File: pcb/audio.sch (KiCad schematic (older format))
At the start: 32 parts, among them J1 AudioJack3_SwitchTR, U400 CS43130, U401 ADP150-3.0, U402 ADP150-1.8, U403 ADP150-1.8, X400 DSC1001CE2-022.5792

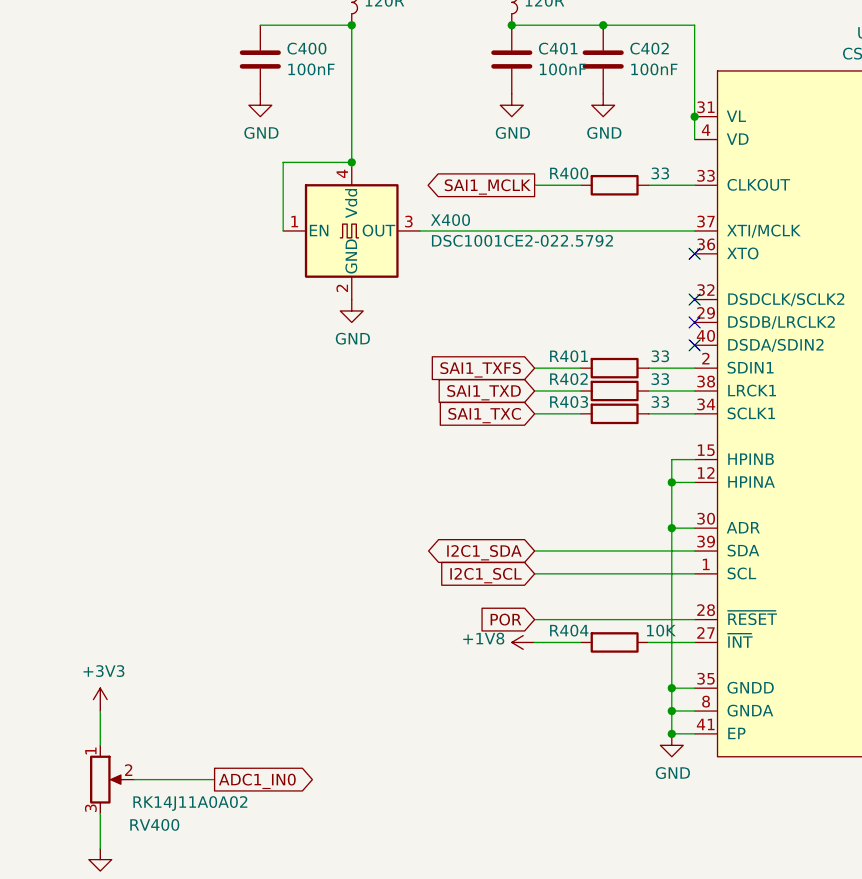
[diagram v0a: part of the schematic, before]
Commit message: pcb: adding lpc5500
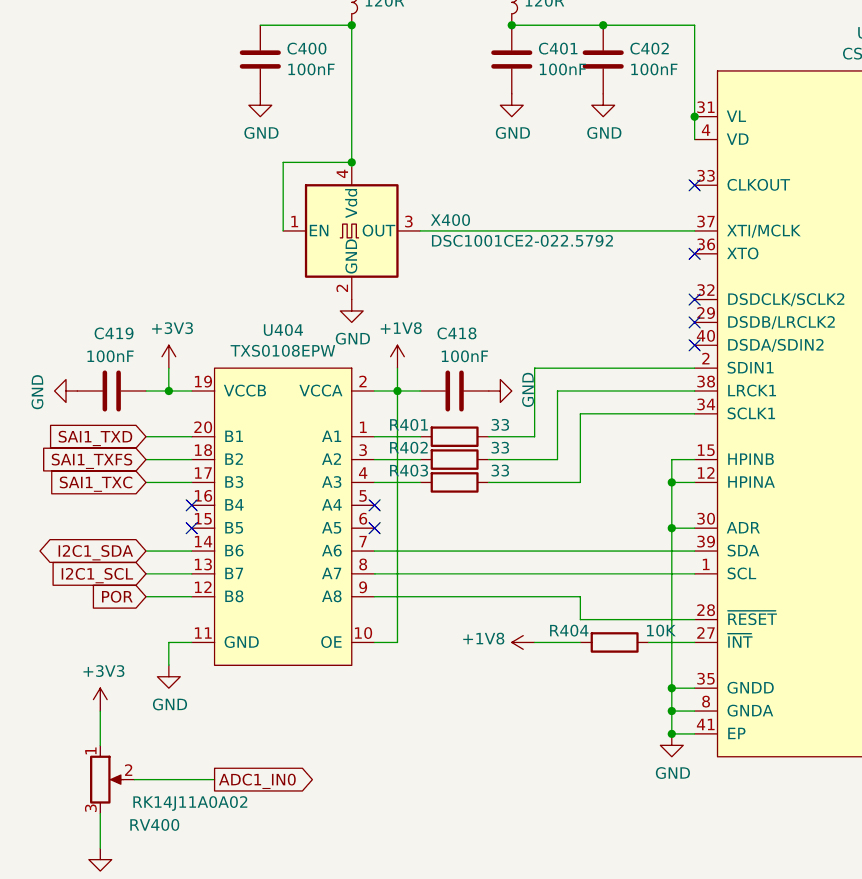
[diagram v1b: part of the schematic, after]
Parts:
- removed R400: 33, Resistor_SMD:R_0603_1608Metric, symbol Device:R
- added C418, C419: 100nF, Capacitor_SMD:C_0402_1005Metric, symbol Device:C
- added U404: TXS0108EPW, Package_SO:TSSOP-20_4.4x6.5mm_P0.65mm, symbol symbols:TXS0108EPW
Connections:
- net +1V8: now also C418.1, U404.10 (OE), U404.2 (VCCA)
- net +3V3: now also C419.2, U404.19 (VCCB)
- net GND: now also C418.2, C419.1, U404.11 (GND)
- net I2C1_SCL: now also U404.13 (B7); no longer U400.1 (SCL)
- net I2C1_SDA: now also U404.14 (B6); no longer U400.39 (SDA)
- net POR: now also U404.12 (B8); no longer U400.28 (~RESET)
- net SAI1_TXC: now also U404.17 (B3); no longer R403.2
- net SAI1_TXD: now also U404.20 (B1); no longer R402.2
- net SAI1_TXFS: now also U404.18 (B2); no longer R401.2
- new net: U400.1 (SCL), U404.8 (A7)
- new net: U400.28 (~RESET), U404.9 (A8)
- new net: U400.39 (SDA), U404.7 (A6)
- new net: R401.2, U404.1 (A1)
- new net: R402.2, U404.3 (A2)
- new net: R403.2, U404.4 (A3)
- no-connect marks 4 -> 9
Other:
- moved on the sheet: R401, R402, R403
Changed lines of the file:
@@
 $Descr A4 11693 8268
 encoding utf-8
-Sheet 7 11
-Title "RhythmPocket"
-Date "2019-08-12"
-Rev "R0.2"
+Sheet 6 8
+Title "RhythmPocketLite"
+Date "2019-09-06"
+Rev "R0.1"
 Comp "ZephRay"
 Comment1 "zephray@outlook.com"
@@
 Comment4 ""
 $EndDescr
-Text GLabel 4300 4300 0    50   Input ~ 0
+Text GLabel 2600 4600 0    50   Input ~ 0
 SAI1_TXC
-Text GLabel 4300 4100 0    50   Input ~ 0
+Text GLabel 2600 4500 0    50   Input ~ 0
 SAI1_TXFS
-Text GLabel 4300 4200 0    50   Input ~ 0
+Text GLabel 2600 4400 0    50   Input ~ 0
 SAI1_TXD
 $Comp
@@
 	4200 2600 4600 2600
 Connection ~ 4200 2600
-Text GLabel 4300 3300 0    50   Output ~ 0
-SAI1_MCLK
-$Comp
-L Device:R R400
-U 1 1 5D42CABC
-P 4650 3300
-F 0 "R400" V 4600 3100 50  0000 C CNN
-F 1 "33" V 4600 3500 50  0000 C CNN
-F 2 "Resistor_SMD:R_0603_1608Metric" V 4580 3300 50  0001 C CNN
-F 3 "~" H 4650 3300 50  0001 C CNN
-	1    4650 3300
-	0    1    1    0
-$EndComp
 $Comp
 L Device:R R401
 U 1 1 5D437A63
-P 4650 4100
-F 0 "R401" V 4600 3900 50  0000 C CNN
-F 1 "33" V 4600 4300 50  0000 C CNN
-F 2 "Resistor_SMD:R_0603_1608Metric" V 4580 4100 50  0001 C CNN
-F 3 "~" H 4650 4100 50  0001 C CNN
-	1    4650 4100
+P 3950 4400
+F 0 "R401" V 3900 4200 50  0000 C CNN
+F 1 "33" V 3900 4600 50  0000 C CNN
+F 2 "Resistor_SMD:R_0603_1608Metric" V 3880 4400 50  0001 C CNN
+F 3 "~" H 3950 4400 50  0001 C CNN
+	1    3950 4400
 	0    1    1    0
 $EndComp
@@
 L Device:R R402
 U 1 1 5D438FF1
-P 4650 4200
-F 0 "R402" V 4600 4000 50  0000 C CNN
-F 1 "33" V 4600 4400 50  0000 C CNN
-F 2 "Resistor_SMD:R_0603_1608Metric" V 4580 4200 50  0001 C CNN
-F 3 "~" H 4650 4200 50  0001 C CNN
-	1    4650 4200
+P 3950 4500
+F 0 "R402" V 3900 4300 50  0000 C CNN
+F 1 "33" V 3900 4700 50  0000 C CNN
+F 2 "Resistor_SMD:R_0603_1608Metric" V 3880 4500 50  0001 C CNN
+F 3 "~" H 3950 4500 50  0001 C CNN
+	1    3950 4500
 	0    1    1    0
 $EndComp
@@
 L Device:R R403
 U 1 1 5D4391CB
-P 4650 4300
-F 0 "R403" V 4600 4100 50  0000 C CNN
-F 1 "33" V 4600 4500 50  0000 C CNN
-F 2 "Resistor_SMD:R_0603_1608Metric" V 4580 4300 50  0001 C CNN
-F 3 "~" H 4650 4300 50  0001 C CNN
-	1    4650 4300
+P 3950 4600
+F 0 "R403" V 3900 4400 50  0000 C CNN
+F 1 "33" V 3900 4800 50  0000 C CNN
+F 2 "Resistor_SMD:R_0603_1608Metric" V 3880 4600 50  0001 C CNN
+F 3 "~" H 3950 4600 50  0001 C CNN
+	1    3950 4600
 	0    1    1    0
 $EndComp
@@
 	5000 3000 5000 3100
 Wire Wire Line
-	4300 4100 4500 4100
-Wire Wire Line
-	4300 4200 4500 4200
-Wire Wire Line
-	4300 4300 4500 4300
-Wire Wire Line
-	4300 3300 4500 3300
-Wire Wire Line
-	4800 3300 5000 3300
-Wire Wire Line
-	4800 4100 5000 4100
-Wire Wire Line
-	4800 4200 5000 4200
-Wire Wire Line
-	4800 4300 5000 4300
-$Comp
-L power:GND #PWR0270
-U 1 1 5D44FB8A
-P 4900 5700
-F 0 "#PWR0270" H 4900 5450 50  0001 C CNN
-F 1 "GND" H 4905 5527 50  0000 C CNN
-F 2 "" H 4900 5700 50  0001 C CNN
-F 3 "" H 4900 5700 50  0001 C CNN
-	1    4900 5700
-	1    0    0    -1
-$EndComp
+	3600 4400 3800 4400
+Wire Wire Line
+	3600 4500 3800 4500
+Wire Wire Line
+	3600 4600 3800 4600
+Wire Wire Line
+	4100 4400 4300 4400
 Wire Wire Line
 	5000 4800 4900 4800
@@
 Wire Wire Line
 	4900 5600 4900 5700
-Wire Wire Line
-	5000 4500 4900 4500
-Wire Wire Line
-	4900 4500 4900 4600
 Connection ~ 4900 4800
 Wire Wire Line
 	5000 4600 4900 4600
-Connection ~ 4900 4600
 Wire Wire Line
 	4900 4600 4900 4800
-Text GLabel 4300 5000 0    50   Input ~ 0
+Text GLabel 2600 5000 0    50   Input ~ 0
 I2C1_SCL
-Text GLabel 4300 4900 0    50   BiDi ~ 0
+Text GLabel 2600 4900 0    50   BiDi ~ 0
 I2C1_SDA
-Wire Wire Line
-	4300 4900 5000 4900
-Wire Wire Line
-	4300 5000 5000 5000
-Text GLabel 4300 5200 0    50   Input ~ 0
+Text GLabel 2600 5100 0    50   Input ~ 0
 POR
-Wire Wire Line
-	4300 5200 5000 5200
 $Comp
 L Device:R R404
@@
 Wire Wire Line
 	6600 5400 7650 5400
+NoConn ~ 5000 3300
+$Comp
+L symbols:TXS0108EPW U404
+U 1 1 5D795725
+P 3200 4400
+F 0 "U404" H 3200 4865 50  0000 C CNN
+F 1 "TXS0108EPW" H 3200 4774 50  0000 C CNN
+F 2 "Package_SO:TSSOP-20_4.4x6.5mm_P0.65mm" H 3200 4400 50  0001 C CNN
+F 3 "" H 3200 4400 50  0001 C CNN
+	1    3200 4400
+	-1   0    0    -1
+$EndComp
+Wire Wire Line
+	2600 4400 2800 4400
+Wire Wire Line
+	2600 4500 2800 4500
+Wire Wire Line
+	2600 4600 2800 4600
+Wire Wire Line
+	4300 4400 4300 4100
+Wire Wire Line
+	4300 4100 5000 4100
+Wire Wire Line
+	5000 4200 4400 4200
+Wire Wire Line
+	4400 4200 4400 4500
+Wire Wire Line
+	4100 4500 4400 4500
+Wire Wire Line
+	4500 4600 4500 4300
+Wire Wire Line
+	4500 4300 5000 4300
+Wire Wire Line
+	4100 4600 4500 4600
+Wire Wire Line
+	5000 4500 4900 4500
+Wire Wire Line
+	4900 4500 4900 4600
+Connection ~ 4900 4600
+Wire Wire Line
+	2600 4900 2800 4900
+Wire Wire Line
+	2600 5000 2800 5000
+Wire Wire Line
+	2600 5100 2800 5100
+Wire Wire Line
+	3600 4900 5000 4900
+Wire Wire Line
+	3600 5000 5000 5000
+Wire Wire Line
+	5000 5200 4500 5200
+Wire Wire Line
+	4500 5200 4500 5100
+Wire Wire Line
+	4500 5100 3600 5100
+NoConn ~ 3600 4700
+NoConn ~ 3600 4800
+NoConn ~ 2800 4700
+NoConn ~ 2800 4800
+$Comp
+L power:+1V8 #PWR?
+U 1 1 5D818AFA
+P 3700 4100
+F 0 "#PWR?" H 3700 3950 50  0001 C CNN
+F 1 "+1V8" H 3715 4273 50  0000 C CNN
+F 2 "" H 3700 4100 50  0001 C CNN
+F 3 "" H 3700 4100 50  0001 C CNN
+	1    3700 4100
+	1    0    0    -1
+$EndComp
+Wire Wire Line
+	3600 4200 3700 4200
+Wire Wire Line
+	3700 4200 3700 4100
+Wire Wire Line
+	3600 5300 3700 5300
+Wire Wire Line
+	3700 5300 3700 4200
+Connection ~ 3700 4200
+$Comp
+L power:+3V3 #PWR?
+U 1 1 5D825A06
+P 2700 4100
+F 0 "#PWR?" H 2700 3950 50  0001 C CNN
+F 1 "+3V3" H 2715 4273 50  0000 C CNN
+F 2 "" H 2700 4100 50  0001 C CNN
+F 3 "" H 2700 4100 50  0001 C CNN
+	1    2700 4100
+	1    0    0    -1
+$EndComp
+Wire Wire Line
+	2700 4100 2700 4200
+Wire Wire Line
+	2700 4200 2800 4200
+$Comp
+L power:GND #PWR0270
+U 1 1 5D44FB8A
+P 4900 5700
+F 0 "#PWR0270" H 4900 5450 50  0001 C CNN
+F 1 "GND" H 4905 5527 50  0000 C CNN
+F 2 "" H 4900 5700 50  0001 C CNN
+F 3 "" H 4900 5700 50  0001 C CNN
+	1    4900 5700
+	1    0    0    -1
+$EndComp
+$Comp
+L power:GND #PWR?
+U 1 1 5D830E8D
+P 2700 5400
+F 0 "#PWR?" H 2700 5150 50  0001 C CNN
+F 1 "GND" H 2705 5227 50  0000 C CNN
+F 2 "" H 2700 5400 50  0001 C CNN
+F 3 "" H 2700 5400 50  0001 C CNN
+	1    2700 5400
+	1    0    0    -1
+$EndComp
+Wire Wire Line
+	2800 5300 2700 5300
+Wire Wire Line
+	2700 5300 2700 5400
+$Comp
+L Device:C C418
+U 1 1 5D83653A
+P 3950 4200
+F 0 "C418" V 4200 4100 50  0000 L CNN
+F 1 "100nF" V 4100 4050 50  0000 L CNN
+F 2 "Capacitor_SMD:C_0402_1005Metric" H 3988 4050 50  0001 C CNN
+F 3 "~" H 3950 4200 50  0001 C CNN
+	1    3950 4200
+	0    -1   -1   0
+$EndComp
+$Comp
+L Device:C C419
+U 1 1 5D83DFEF
+P 2450 4200
+F 0 "C419" V 2700 4100 50  0000 L CNN
+F 1 "100nF" V 2600 4100 50  0000 L CNN
+F 2 "Capacitor_SMD:C_0402_1005Metric" H 2488 4050 50  0001 C CNN
+F 3 "~" H 2450 4200 50  0001 C CNN
+	1    2450 4200
+	0    -1   -1   0
+$EndComp
+Wire Wire Line
+	2600 4200 2700 4200
+Connection ~ 2700 4200
+Wire Wire Line
+	3800 4200 3700 4200
+$Comp
+L power:GND #PWR?
+U 1 1 5D84AB6D
+P 4100 4200
+F 0 "#PWR?" H 4100 3950 50  0001 C CNN
+F 1 "GND" H 4105 4027 50  0000 C CNN
+F 2 "" H 4100 4200 50  0001 C CNN
+F 3 "" H 4100 4200 50  0001 C CNN
+	1    4100 4200
+	0    -1   -1   0
+$EndComp
+$Comp
+L power:GND #PWR?
+U 1 1 5D84B27D
+P 2300 4200
+F 0 "#PWR?" H 2300 3950 50  0001 C CNN
+F 1 "GND" H 2305 4027 50  0000 C CNN
+F 2 "" H 2300 4200 50  0001 C CNN
+F 3 "" H 2300 4200 50  0001 C CNN
+	1    2300 4200
+	0    1    1    0
+$EndComp
 $EndSCHEMATC

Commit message: pcb: rev 0.1
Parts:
- removed C418, C419: 100nF, Capacitor_SMD:C_0402_1005Metric, symbol Device:C
- removed U404: TXS0108EPW, Package_SO:TSSOP-20_4.4x6.5mm_P0.65mm, symbol symbols:TXS0108EPW
- removed X400: DSC1001CE2-022.5792, Oscillator:Oscillator_SMD_Abracon_ASE-4Pin_3.2x2.5mm, symbol Oscillator:ASE-xxxMHz
- added R400: 33, Resistor_SMD:R_0603_1608Metric, symbol Device:R
- added X1: DSC1001CE2-022.5792, Oscillator:Oscillator_SMD_Abracon_ASE-4Pin_3.2x2.5mm, symbol Oscillator:ASE-xxxMHz
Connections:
- net +1V8: now also RV400.1
- net +3V3: no longer RV400.1
- net GND: now also X1.2 (GND)
- net I2C1_SCL: now also U400.1 (SCL)
- net I2C1_SDA: now also U400.39 (SDA)
- net POR: now also U400.28 (~RESET)
- net SAI1_TXC: now also R403.2
- net SAI1_TXD: now also R401.2
- net SAI1_TXFS: now also R402.2
- net at U400.33 (CLKOUT): now also R400.1
- net at U400.37 (XTI/MCLK): now also X1.3 (OUT)
- net at C400.1, L400.2: now also X1.1 (EN), X1.4 (Vdd)
- new net SAI1_MCLK: R400.2
- no-connect marks 9 -> 4
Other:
- moved on the sheet: R401, R402, R403
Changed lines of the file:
@@
 Comment4 ""
 $EndDescr
-Text GLabel 2600 4600 0    50   Input ~ 0
-SAI1_TXC
-Text GLabel 2600 4500 0    50   Input ~ 0
-SAI1_TXFS
-Text GLabel 2600 4400 0    50   Input ~ 0
-SAI1_TXD
 $Comp
 L symbols:CS43130 U400
@@
 L Device:R R401
 U 1 1 5D437A63
-P 3950 4400
-F 0 "R401" V 3900 4200 50  0000 C CNN
-F 1 "33" V 3900 4600 50  0000 C CNN
-F 2 "Resistor_SMD:R_0603_1608Metric" V 3880 4400 50  0001 C CNN
-F 3 "~" H 3950 4400 50  0001 C CNN
-	1    3950 4400
+P 3950 4100
+F 0 "R401" V 3900 3900 50  0000 C CNN
+F 1 "33" V 3900 4300 50  0000 C CNN
+F 2 "Resistor_SMD:R_0603_1608Metric" V 3880 4100 50  0001 C CNN
+F 3 "~" H 3950 4100 50  0001 C CNN
+	1    3950 4100
 	0    1    1    0
 $EndComp
@@
 L Device:R R402
 U 1 1 5D438FF1
-P 3950 4500
-F 0 "R402" V 3900 4300 50  0000 C CNN
-F 1 "33" V 3900 4700 50  0000 C CNN
-F 2 "Resistor_SMD:R_0603_1608Metric" V 3880 4500 50  0001 C CNN
-F 3 "~" H 3950 4500 50  0001 C CNN
-	1    3950 4500
+P 3950 4200
+F 0 "R402" V 3900 4000 50  0000 C CNN
+F 1 "33" V 3900 4400 50  0000 C CNN
+F 2 "Resistor_SMD:R_0603_1608Metric" V 3880 4200 50  0001 C CNN
+F 3 "~" H 3950 4200 50  0001 C CNN
+	1    3950 4200
 	0    1    1    0
 $EndComp
@@
 L Device:R R403
 U 1 1 5D4391CB
-P 3950 4600
-F 0 "R403" V 3900 4400 50  0000 C CNN
-F 1 "33" V 3900 4800 50  0000 C CNN
-F 2 "Resistor_SMD:R_0603_1608Metric" V 3880 4600 50  0001 C CNN
-F 3 "~" H 3950 4600 50  0001 C CNN
-	1    3950 4600
+P 3950 4300
+F 0 "R403" V 3900 4100 50  0000 C CNN
+F 1 "33" V 3900 4500 50  0000 C CNN
+F 2 "Resistor_SMD:R_0603_1608Metric" V 3880 4300 50  0001 C CNN
+F 3 "~" H 3950 4300 50  0001 C CNN
+	1    3950 4300
 	0    1    1    0
 $EndComp
@@
 	5000 3000 5000 3100
 Wire Wire Line
-	3600 4400 3800 4400
-Wire Wire Line
-	3600 4500 3800 4500
-Wire Wire Line
-	3600 4600 3800 4600
-Wire Wire Line
-	4100 4400 4300 4400
-Wire Wire Line
 	5000 4800 4900 4800
 Wire Wire Line
@@
 Wire Wire Line
 	4900 4600 4900 4800
-Text GLabel 2600 5000 0    50   Input ~ 0
-I2C1_SCL
-Text GLabel 2600 4900 0    50   BiDi ~ 0
-I2C1_SDA
-Text GLabel 2600 5100 0    50   Input ~ 0
-POR
 $Comp
 L Device:R R404
@@
 NoConn ~ 5000 3600
 $Comp
-L Oscillator:ASE-xxxMHz X400
-U 1 1 5D484130
-P 3500 3500
-F 0 "X400" H 3844 3546 50  0000 L CNN
-F 1 "DSC1001CE2-022.5792" H 3844 3455 50  0000 L CNN
-F 2 "Oscillator:Oscillator_SMD_Abracon_ASE-4Pin_3.2x2.5mm" H 4200 3150 50  0001 C CNN
-F 3 "http://www.abracon.com/Oscillators/ASV.pdf" H 3400 3500 50  0001 C CNN
-	1    3500 3500
-	1    0    0    -1
-$EndComp
-$Comp
 L power:+1V8 #PWR0272
 U 1 1 5D485FE4
@@
 Wire Wire Line
 	3200 3200 3500 3200
-Connection ~ 3500 3200
 Wire Wire Line
 	3800 3500 5000 3500
@@
 	1    0    0    -1
 $EndComp
-$Comp
-L power:+3V3 #PWR0276
-U 1 1 5D1F4C5C
-P 2400 5600
-F 0 "#PWR0276" H 2400 5450 50  0001 C CNN
-F 1 "+3V3" H 2415 5773 50  0000 C CNN
-F 2 "" H 2400 5600 50  0001 C CNN
-F 3 "" H 2400 5600 50  0001 C CNN
-	1    2400 5600
-	1    0    0    -1
-$EndComp
 Wire Wire Line
 	2400 6050 2400 6200
@@
 Wire Wire Line
 	6600 5400 7650 5400
-NoConn ~ 5000 3300
-$Comp
-L symbols:TXS0108EPW U404
-U 1 1 5D795725
-P 3200 4400
-F 0 "U404" H 3200 4865 50  0000 C CNN
-F 1 "TXS0108EPW" H 3200 4774 50  0000 C CNN
-F 2 "Package_SO:TSSOP-20_4.4x6.5mm_P0.65mm" H 3200 4400 50  0001 C CNN
-F 3 "" H 3200 4400 50  0001 C CNN
-	1    3200 4400
-	-1   0    0    -1
-$EndComp
-Wire Wire Line
-	2600 4400 2800 4400
-Wire Wire Line
-	2600 4500 2800 4500
-Wire Wire Line
-	2600 4600 2800 4600
-Wire Wire Line
-	4300 4400 4300 4100
-Wire Wire Line
-	4300 4100 5000 4100
-Wire Wire Line
-	5000 4200 4400 4200
-Wire Wire Line
-	4400 4200 4400 4500
-Wire Wire Line
-	4100 4500 4400 4500
-Wire Wire Line
-	4500 4600 4500 4300
-Wire Wire Line
-	4500 4300 5000 4300
-Wire Wire Line
-	4100 4600 4500 4600
 Wire Wire Line
 	5000 4500 4900 4500
@@
 	4900 4500 4900 4600
 Connection ~ 4900 4600
-Wire Wire Line
-	2600 4900 2800 4900
-Wire Wire Line
-	2600 5000 2800 5000
-Wire Wire Line
-	2600 5100 2800 5100
-Wire Wire Line
-	3600 4900 5000 4900
-Wire Wire Line
-	3600 5000 5000 5000
-Wire Wire Line
-	5000 5200 4500 5200
-Wire Wire Line
-	4500 5200 4500 5100
-Wire Wire Line
-	4500 5100 3600 5100
-NoConn ~ 3600 4700
-NoConn ~ 3600 4800
-NoConn ~ 2800 4700
-NoConn ~ 2800 4800
-$Comp
-L power:+1V8 #PWR?
-U 1 1 5D818AFA
-P 3700 4100
-F 0 "#PWR?" H 3700 3950 50  0001 C CNN
-F 1 "+1V8" H 3715 4273 50  0000 C CNN
-F 2 "" H 3700 4100 50  0001 C CNN
-F 3 "" H 3700 4100 50  0001 C CNN
-	1    3700 4100
-	1    0    0    -1
-$EndComp
-Wire Wire Line
-	3600 4200 3700 4200
-Wire Wire Line
-	3700 4200 3700 4100
-Wire Wire Line
-	3600 5300 3700 5300
-Wire Wire Line
-	3700 5300 3700 4200
-Connection ~ 3700 4200
-$Comp
-L power:+3V3 #PWR?
-U 1 1 5D825A06
-P 2700 4100
-F 0 "#PWR?" H 2700 3950 50  0001 C CNN
-F 1 "+3V3" H 2715 4273 50  0000 C CNN
-F 2 "" H 2700 4100 50  0001 C CNN
-F 3 "" H 2700 4100 50  0001 C CNN
-	1    2700 4100
-	1    0    0    -1
-$EndComp
-Wire Wire Line
-	2700 4100 2700 4200
-Wire Wire Line
-	2700 4200 2800 4200
 $Comp
 L power:GND #PWR0270
@@
 	1    0    0    -1
 $EndComp
-$Comp
-L power:GND #PWR?
-U 1 1 5D830E8D
-P 2700 5400
-F 0 "#PWR?" H 2700 5150 50  0001 C CNN
-F 1 "GND" H 2705 5227 50  0000 C CNN
-F 2 "" H 2700 5400 50  0001 C CNN
-F 3 "" H 2700 5400 50  0001 C CNN
-	1    2700 5400
-	1    0    0    -1
-$EndComp
-Wire Wire Line
-	2800 5300 2700 5300
-Wire Wire Line
-	2700 5300 2700 5400
-$Comp
-L Device:C C418
-U 1 1 5D83653A
-P 3950 4200
-F 0 "C418" V 4200 4100 50  0000 L CNN
-F 1 "100nF" V 4100 4050 50  0000 L CNN
-F 2 "Capacitor_SMD:C_0402_1005Metric" H 3988 4050 50  0001 C CNN
-F 3 "~" H 3950 4200 50  0001 C CNN
-	1    3950 4200
-	0    -1   -1   0
-$EndComp
-$Comp
-L Device:C C419
-U 1 1 5D83DFEF
-P 2450 4200
-F 0 "C419" V 2700 4100 50  0000 L CNN
-F 1 "100nF" V 2600 4100 50  0000 L CNN
-F 2 "Capacitor_SMD:C_0402_1005Metric" H 2488 4050 50  0001 C CNN
-F 3 "~" H 2450 4200 50  0001 C CNN
-	1    2450 4200
-	0    -1   -1   0
-$EndComp
-Wire Wire Line
-	2600 4200 2700 4200
-Connection ~ 2700 4200
-Wire Wire Line
-	3800 4200 3700 4200
-$Comp
-L power:GND #PWR?
-U 1 1 5D84AB6D
-P 4100 4200
-F 0 "#PWR?" H 4100 3950 50  0001 C CNN
-F 1 "GND" H 4105 4027 50  0000 C CNN
-F 2 "" H 4100 4200 50  0001 C CNN
-F 3 "" H 4100 4200 50  0001 C CNN
-	1    4100 4200
-	0    -1   -1   0
-$EndComp
-$Comp
-L power:GND #PWR?
-U 1 1 5D84B27D
-P 2300 4200
-F 0 "#PWR?" H 2300 3950 50  0001 C CNN
-F 1 "GND" H 2305 4027 50  0000 C CNN
-F 2 "" H 2300 4200 50  0001 C CNN
-F 3 "" H 2300 4200 50  0001 C CNN
-	1    2300 4200
-	0    1    1    0
+Text GLabel 3400 4300 0    50   Input ~ 0
+SAI1_TXC
+Text GLabel 3400 4200 0    50   Input ~ 0
+SAI1_TXFS
+Text GLabel 3400 4100 0    50   Input ~ 0
+SAI1_TXD
+Text GLabel 3400 5000 0    50   Input ~ 0
+I2C1_SCL
+Text GLabel 3400 4900 0    50   BiDi ~ 0
+I2C1_SDA
+Text GLabel 3400 5200 0    50   Input ~ 0
+POR
+Wire Wire Line
+	3400 4100 3800 4100
+Wire Wire Line
+	3400 4200 3800 4200
+Wire Wire Line
+	3400 4300 3800 4300
+Wire Wire Line
+	3400 4900 5000 4900
+Wire Wire Line
+	3400 5000 5000 5000
+$Comp
+L Oscillator:ASE-xxxMHz X1
+U 1 1 5D80F8A2
+P 3500 3500
+AR Path="/5D438133/5D80F8A2" Ref="X1"  Part="1"
+AR Path="/5DB2122B/5D80F8A2" Ref="X?"  Part="1"
+F 0 "X1" H 3844 3546 50  0000 L CNN
+F 1 "DSC1001CE2-022.5792" H 3844 3455 50  0000 L CNN
+F 2 "Oscillator:Oscillator_SMD_Abracon_ASE-4Pin_3.2x2.5mm" H 4200 3150 50  0001 C CNN
+F 3 "http://www.abracon.com/Oscillators/ASV.pdf" H 3400 3500 50  0001 C CNN
+	1    3500 3500
+	1    0    0    -1
+$EndComp
+Wire Wire Line
+	3400 5200 5000 5200
+Wire Wire Line
+	4100 4100 5000 4100
+Wire Wire Line
+	4100 4200 5000 4200
+Wire Wire Line
+	4100 4300 5000 4300
+Text GLabel 4400 3300 0    50   Output ~ 0
+SAI1_MCLK
+$Comp
+L Device:R R400
+U 1 1 5D92452D
+P 4750 3300
+F 0 "R400" V 4700 3100 50  0000 C CNN
+F 1 "33" V 4700 3500 50  0000 C CNN
+F 2 "Resistor_SMD:R_0603_1608Metric" V 4680 3300 50  0001 C CNN
+F 3 "~" H 4750 3300 50  0001 C CNN
+	1    4750 3300
+	0    1    1    0
+$EndComp
+Wire Wire Line
+	4900 3300 5000 3300
+Wire Wire Line
+	4600 3300 4400 3300
+$Comp
+L power:+1V8 #PWR0102
+U 1 1 5D77A87B
+P 2400 5600
+F 0 "#PWR0102" H 2400 5450 50  0001 C CNN
+F 1 "+1V8" H 2415 5773 50  0000 C CNN
+F 2 "" H 2400 5600 50  0001 C CNN
+F 3 "" H 2400 5600 50  0001 C CNN
+	1    2400 5600
+	1    0    0    -1
 $EndComp
 $EndSCHEMATC
